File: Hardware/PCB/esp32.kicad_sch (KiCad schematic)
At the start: 10 parts, among them J18 Programmer, U11 ESP32-S3-WROOM-1U-N16R8

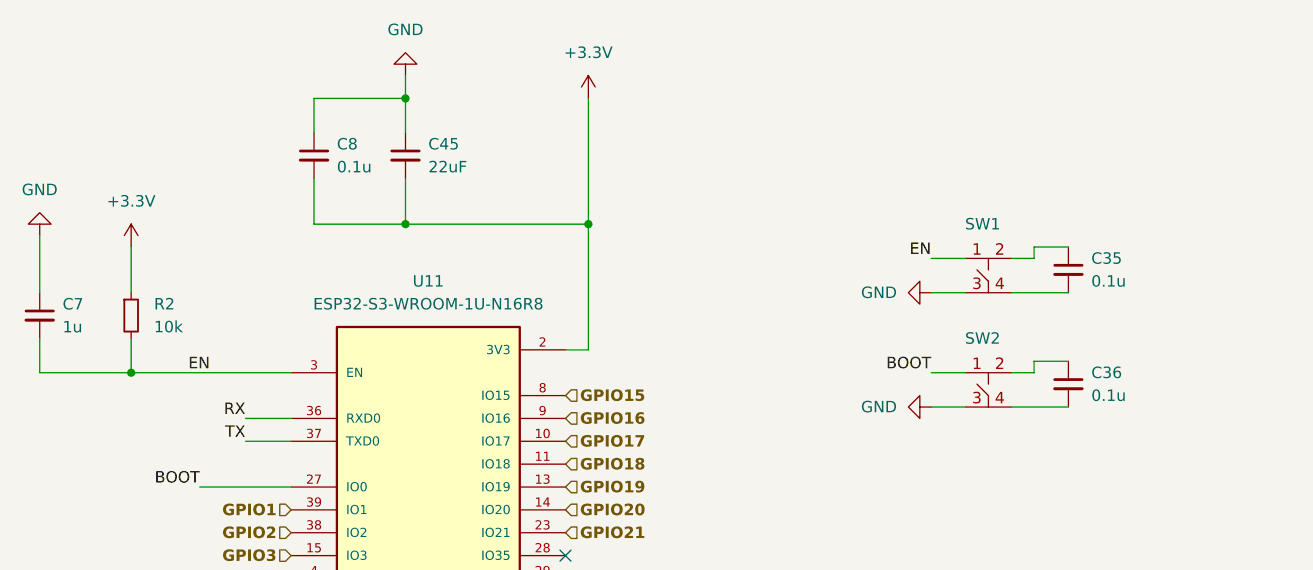
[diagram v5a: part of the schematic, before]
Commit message: fixed BOM, added some silkscreen, getting quote now
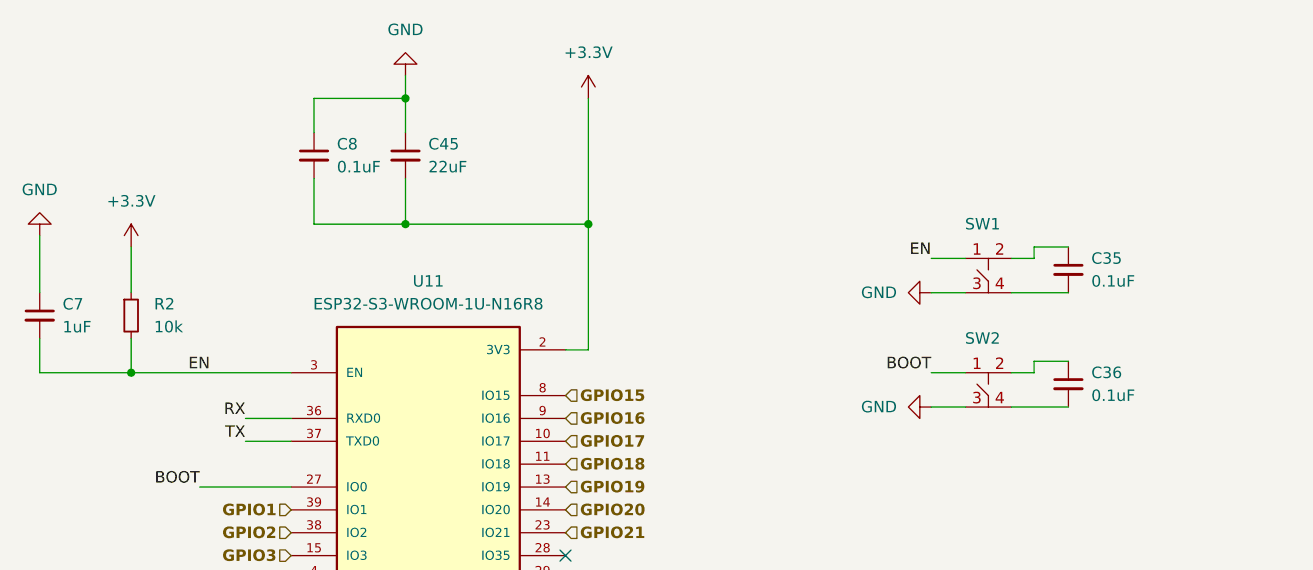
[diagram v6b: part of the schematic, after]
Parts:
- C35, C36, C8: value 0.1u -> 0.1uF
- C7: value 1u -> 1uF; DigiKey Link https://www.digikey.com/en/products/detail/samsung-electro-mechanics/CL10B105KP8NNNC/3887604 -> https://www.digikey.com/en/products/detail/samsung-electro-mechanics/CL10B105KO8NNNC/3886677; MPN CL10B105KP8NNNC -> CL10B105KO8NNNC
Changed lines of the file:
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@@
 			)
 		)
-		(property "Value" "0.1u"
+		(property "Value" "0.1uF"
 			(at 160.02 66.0462 0)
 			(effects
@@
 			)
 		)
-		(property "Value" "1u"
+		(property "Value" "1uF"
 			(at 45.72 71.1262 0)
 			(effects
@@
 			)
 		)
-		(property "Description" "1 µF ±10% 10V Ceramic Capacitor X7R 0603 (1608 Metric)"
+		(property "Description" "1 µF ±10% 16V Ceramic Capacitor X7R 0603 (1608 Metric)"
 			(at 43.18 69.85 0)
 			(effects
@@
 			)
 		)
-		(property "DigiKey Link" "https://www.digikey.com/en/products/detail/samsung-electro-mechanics/CL10B105KP8NNNC/3887604"
+		(property "DigiKey Link" "https://www.digikey.com/en/products/detail/samsung-electro-mechanics/CL10B105KO8NNNC/3886677"
 			(at 43.18 69.85 0)
 			(effects
@@
 			)
 		)
-		(property "MPN" "CL10B105KP8NNNC"
+		(property "MPN" "CL10B105KO8NNNC"
 			(at 43.18 69.85 0)
 			(effects
@@
 			)
 		)
-		(property "Value" "0.1u"
+		(property "Value" "0.1uF"
 			(at 160.02 78.7462 0)
 			(effects
@@
 			)
 		)
-		(property "Value" "0.1u"
+		(property "Value" "0.1uF"
 			(at 76.2 53.3462 0)
 			(effects

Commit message: kinda pricey, I should try to make a smaller version using LCSC parts for cheaper solution
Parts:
- C35, C36, C8: LCSC (none) -> C66501
- C45: LCSC (none) -> C398815
- C7: LCSC (none) -> C59782
- J18: LCSC (none) -> C5372863
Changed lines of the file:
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@@
+			)
+		)
+		(property "LCSC" "C66501"
+			(at 157.48 64.77 0)
+			(effects
+				(font
+					(size 1.27 1.27)
+				)
 			)
 		)
@@
 			)
 		)
+		(property "LCSC" ""
+			(at 53.34 69.85 0)
+			(effects
+				(font
+					(size 1.27 1.27)
+				)
+			)
+		)
 		(pin "1"
 		)
@@
 			)
 		)
+		(property "LCSC" ""
+			(at 148.59 63.5 0)
+			(effects
+				(font
+					(size 1.27 1.27)
+				)
+			)
+		)
 		(pin "3"
 		)
@@
 			)
 		)
+		(property "LCSC" "C59782"
+			(at 43.18 69.85 0)
+			(effects
+				(font
+					(size 1.27 1.27)
+				)
+			)
+		)
 		(pin "2"
 		)
@@
 			)
 		)
+		(property "LCSC" "C398815"
+			(at 83.82 52.07 0)
+			(effects
+				(font
+					(size 1.27 1.27)
+				)
+			)
+		)
 		(pin "2"
 		)
@@
 			)
 		)
+		(property "LCSC" ""
+			(at 86.36 101.6 0)
+			(effects
+				(font
+					(size 1.27 1.27)
+				)
+			)
+		)
 		(pin "9"
 		)
@@
 			)
 		)
+		(property "LCSC" "C5372863"
+			(at 194.31 137.16 0)
+			(effects
+				(font
+					(size 1.27 1.27)
+				)
+			)
+		)
 		(pin "2"
 		)
@@
 			)
 		)
+		(property "LCSC" "C66501"
+			(at 157.48 77.47 0)
+			(effects
+				(font
+					(size 1.27 1.27)
+				)
+			)
+		)
 		(pin "2"
 		)
@@
 			)
 		)
+		(property "LCSC" "C66501"
+			(at 73.66 52.07 0)
+			(effects
+				(font
+					(size 1.27 1.27)
+				)
+			)
+		)
 		(pin "2"
 		)
@@
 			)
 		)
+		(property "LCSC" ""
+			(at 148.59 76.2 0)
+			(effects
+				(font
+					(size 1.27 1.27)
+				)
+			)
+		)

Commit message: done with this, placed order
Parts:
- removed C35, C36: 0.1uF, Capacitor_SMD:C_0603_1608Metric_Pad1.08x0.95mm_HandSolder, symbol Device:C_Small
- removed SW1, SW2: ~, Vendor_Footprints:PTS647SN50SMTR2LFS, symbol Vendor_Symbols:PTS647SN50SMTR2_LFS
- C45: LCSC C398815 -> C602037; MPN CL21A226MOCLRNC -> CL21A226MAYNNNE
- C7: LCSC C59782 -> C15849; MPN CL10B105KO8NNNC -> CL10A105KB8NNNC
- C8: value 0.1uF -> 100nF; LCSC C66501 -> C14663; MPN CL10B104KO8NNNC -> CC0603KRX7R9BB104; Manufacturer Samsung Electro-Mechanics -> YAGEO
- J18: DigiKey Link https://www.digikey.com/en/products/detail/w%C3%BCrth-elekt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 -> (none); LCSC C5372863 -> C492441; MPN 61200621621 -> XFCN BH254V-6P; Manufacturer Würth Elektronik -> XFCN
- R2: LCSC (none) -> C2930027; MPN RMCF0603JT10K0 -> FRC0603J103TS; Manufacturer Stackpole Electronics Inc -> FOJAN
- U11: DigiKey Link https://www.digikey.com/en/products/detail/espressif-system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 -> (none); LCSC (none) -> C3013946
